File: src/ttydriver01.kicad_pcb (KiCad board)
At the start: 2 copper layers, 119.4 x 74.9 mm, 34 parts, among them P1 CONN_01X04, P2 CONN_01X02, P3 CONN_01X02, P4 CONN_01X10, Q1 IRLB8721PBF, T1 Coilcraft-DA2032, U1 NE555, U2 TPS2030P, U3 CP2102-breakout, U4 G3VM401E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

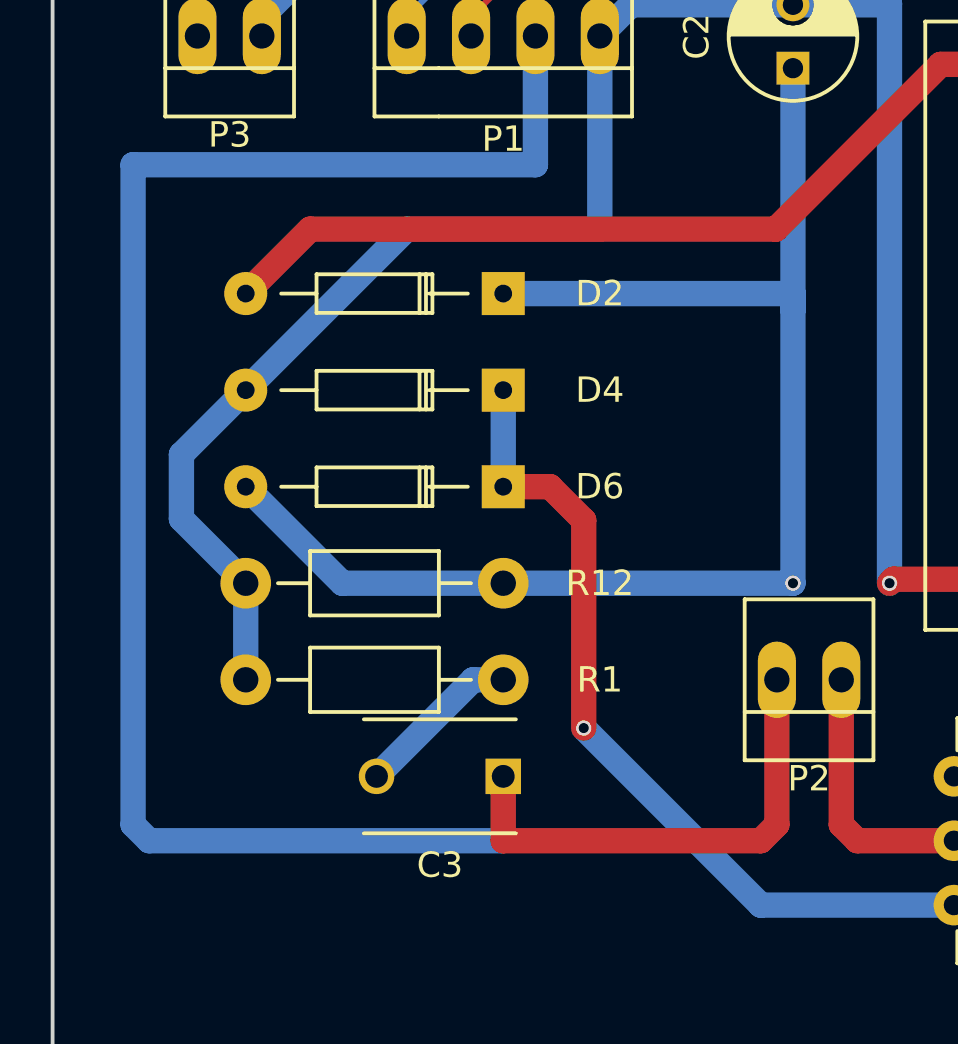
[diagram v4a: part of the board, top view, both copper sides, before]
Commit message: Change resistor R12 to unused R8
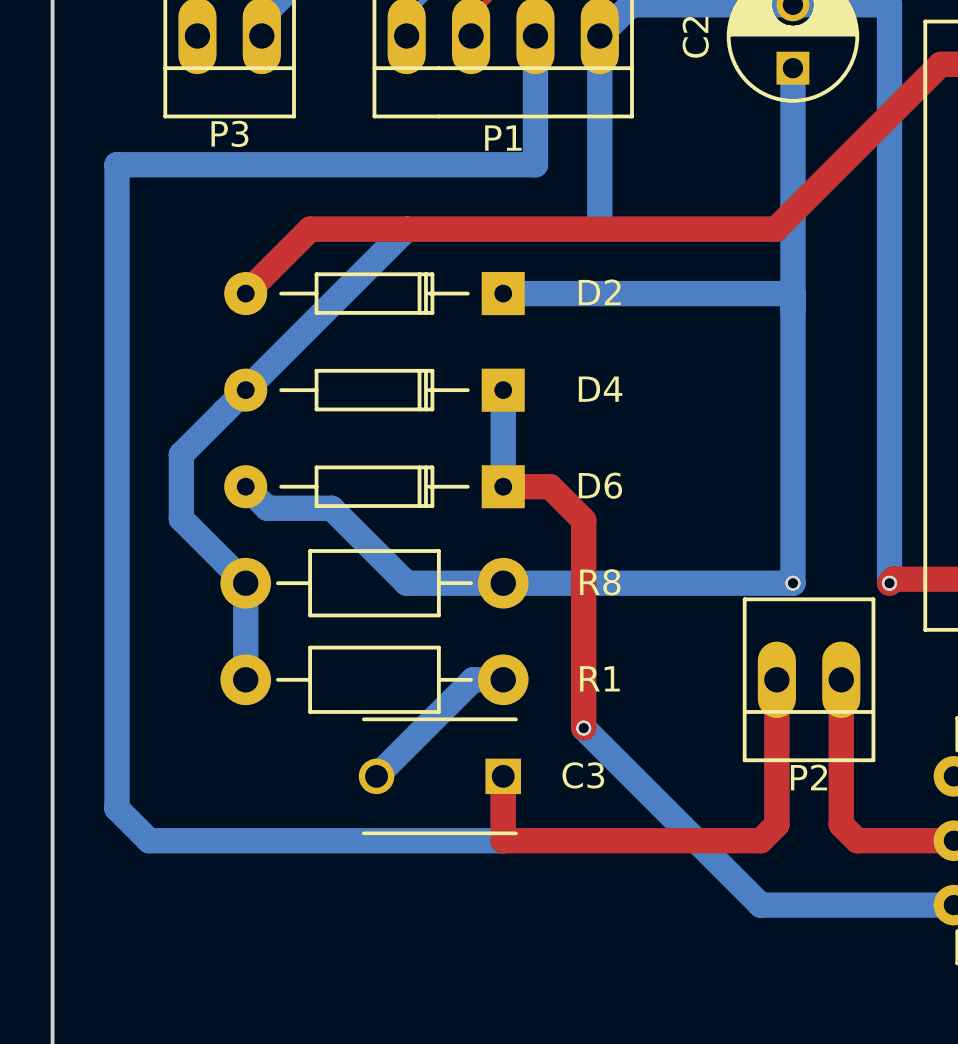
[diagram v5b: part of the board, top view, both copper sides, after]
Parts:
- removed R12: 1M, Resistors_ThroughHole:Resistor_Horizontal_RM10mm
- added R8: 1M, Resistors_ThroughHole:Resistor_Horizontal_RM10mm, F.Cu at (73.7, 130.8)
- R10, R11: value 670 -> 680
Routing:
- net /HVPOS: track 83.7 -> 84.6 mm
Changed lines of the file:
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@@
     (links 78)
     (no_connects 0)
-    (area 55.804999 77.394999 175.335001 152.475001)
+    (area 55.404999 77.394999 193.291156 167.760001)
     (thickness 1.6)
     (drawings 8)
-    (tracks 316)
+    (tracks 319)
     (zones 0)
     (modules 34)
@@
       (effects (font (size 1 1) (thickness 0.15)))
     )
-    (fp_text value 670 (at 5.08 0) (layer F.Fab)
+    (fp_text value 680 (at 5.08 0) (layer F.Fab)
       (effects (font (size 1 1) (thickness 0.15)))
     )
@@
       (effects (font (size 1 1) (thickness 0.15)))
     )
-    (fp_text value 670 (at 5.08 0) (layer F.Fab)
+    (fp_text value 680 (at 5.08 0) (layer F.Fab)
       (effects (font (size 1 1) (thickness 0.15)))
     )
@@
     (pad 2 thru_hole circle (at 10.16 0) (size 1.99898 1.99898) (drill 1.00076) (layers *.Cu *.SilkS *.Mask)
       (net 38 "Net-(P4-Pad9)"))
-    (model Resistors_ThroughHole.3dshapes/Resistor_Horizontal_RM10mm.wrl
-      (at (xyz 0.2 0 0))
-      (scale (xyz 0.4 0.4 0.4))
-      (rotate (xyz 0 0 0))
-    )
-  )
-  (module Resistors_ThroughHole:Resistor_Horizontal_RM10mm (layer F.Cu)
-    (at 73.66 130.81 180)
-    (descr "Resistor, Axial,  RM 10mm, 1/3W")
-    (tags "Resistor Axial RM 10mm 1/3W")
-    (fp_text reference R12 (at -3.81 0 180) (layer F.SilkS)
-      (effects (font (size 1 1) (thickness 0.15)))
-    )
-    (fp_text value 1M (at 5.08 0 180) (layer F.Fab)
-      (effects (font (size 1 1) (thickness 0.15)))
-    )
-    (fp_line (start -1.25 -1.5) (end 11.4 -1.5) (layer F.CrtYd) (width 0.05))
-    (fp_line (start -1.25 1.5) (end -1.25 -1.5) (layer F.CrtYd) (width 0.05))
-    (fp_line (start 11.4 -1.5) (end 11.4 1.5) (layer F.CrtYd) (width 0.05))
-    (fp_line (start -1.25 1.5) (end 11.4 1.5) (layer F.CrtYd) (width 0.05))
-    (fp_line (start 2.54 -1.27) (end 7.62 -1.27) (layer F.SilkS) (width 0.15))
-    (fp_line (start 7.62 -1.27) (end 7.62 1.27) (layer F.SilkS) (width 0.15))
-    (fp_line (start 7.62 1.27) (end 2.54 1.27) (layer F.SilkS) (width 0.15))
-    (fp_line (start 2.54 1.27) (end 2.54 -1.27) (layer F.SilkS) (width 0.15))
-    (fp_line (start 2.54 0) (end 1.27 0) (layer F.SilkS) (width 0.15))
-    (fp_line (start 7.62 0) (end 8.89 0) (layer F.SilkS) (width 0.15))
-    (pad 1 thru_hole circle (at 0 0 180) (size 1.99898 1.99898) (drill 1.00076) (layers *.Cu *.SilkS *.Mask)
-      (net 22 "Net-(C2-Pad1)"))
-    (pad 2 thru_hole circle (at 10.16 0 180) (size 1.99898 1.99898) (drill 1.00076) (layers *.Cu *.SilkS *.Mask)
-      (net 40 /HVNEG))
     (model Resistors_ThroughHole.3dshapes/Resistor_Horizontal_RM10mm.wrl
       (at (xyz 0.2 0 0))
@@
     (descr "Capacitor 6mm Disc, Pitch 5mm")
     (tags Capacitor)
-    (fp_text reference C3 (at 2.5 -3.5 180) (layer F.SilkS)
-      (effects (font (size 1 1) (thickness 0.15)))
-    )
-    (fp_text value 1000pf (at 2.5 3.5 180) (layer F.Fab)
+    (fp_text reference C3 (at -3.175 0 180) (layer F.SilkS)
+      (effects (font (size 1 1) (thickness 0.15)))
+    )
+    (fp_text value 1000pf (at 10.16 0 180) (layer F.Fab)
       (effects (font (size 1 1) (thickness 0.15)))
     )
@@
       (at (xyz 0.0984252 0 0))
       (scale (xyz 1 1 1))
+      (rotate (xyz 0 0 0))
+    )
+  )
+  (module Resistors_ThroughHole:Resistor_Horizontal_RM10mm (layer F.Cu)
+    (at 73.66 130.81 180)
+    (descr "Resistor, Axial,  RM 10mm, 1/3W")
+    (tags "Resistor Axial RM 10mm 1/3W")
+    (fp_text reference R8 (at -3.81 0 180) (layer F.SilkS)
+      (effects (font (size 1 1) (thickness 0.15)))
+    )
+    (fp_text value 1M (at 5.08 0 180) (layer F.Fab)
+      (effects (font (size 1 1) (thickness 0.15)))
+    )
+    (fp_line (start -1.25 -1.5) (end 11.4 -1.5) (layer F.CrtYd) (width 0.05))
+    (fp_line (start -1.25 1.5) (end -1.25 -1.5) (layer F.CrtYd) (width 0.05))
+    (fp_line (start 11.4 -1.5) (end 11.4 1.5) (layer F.CrtYd) (width 0.05))
+    (fp_line (start -1.25 1.5) (end 11.4 1.5) (layer F.CrtYd) (width 0.05))
+    (fp_line (start 2.54 -1.27) (end 7.62 -1.27) (layer F.SilkS) (width 0.15))
+    (fp_line (start 7.62 -1.27) (end 7.62 1.27) (layer F.SilkS) (width 0.15))
+    (fp_line (start 7.62 1.27) (end 2.54 1.27) (layer F.SilkS) (width 0.15))
+    (fp_line (start 2.54 1.27) (end 2.54 -1.27) (layer F.SilkS) (width 0.15))
+    (fp_line (start 2.54 0) (end 1.27 0) (layer F.SilkS) (width 0.15))
+    (fp_line (start 7.62 0) (end 8.89 0) (layer F.SilkS) (width 0.15))
+    (pad 1 thru_hole circle (at 0 0 180) (size 1.99898 1.99898) (drill 1.00076) (layers *.Cu *.SilkS *.Mask)
+      (net 22 "Net-(C2-Pad1)"))
+    (pad 2 thru_hole circle (at 10.16 0 180) (size 1.99898 1.99898) (drill 1.00076) (layers *.Cu *.SilkS *.Mask)
+      (net 40 /HVNEG))
+    (model Resistors_ThroughHole.3dshapes/Resistor_Horizontal_RM10mm.wrl
+      (at (xyz 0.2 0 0))
+      (scale (xyz 0.4 0.4 0.4))
       (rotate (xyz 0 0 0))
     )
@@
   (segment (start 102.81 110.34) (end 105.31 110.34) (width 1) (layer F.Cu) (net 21) (status 30))
   (segment (start 100.31 110.34) (end 102.81 110.34) (width 1) (layer F.Cu) (net 21) (status 30))
+  (segment (start 63.49948 127.00254) (end 64.349109 127.852169) (width 1) (layer B.Cu) (net 22))
   (segment (start 85.09 120.015) (end 85.09 110.49) (width 1) (layer B.Cu) (net 22) (status 20))
-  (via (at 85.09 130.81) (size 0.6) (drill 0.4) (layers F.Cu B.Cu) (net 22))
-  (segment (start 73.66 130.81) (end 67.31 130.81) (width 1) (layer B.Cu) (net 22) (status 10))
-  (segment (start 67.31 130.81) (end 63.50254 127.00254) (width 1) (layer B.Cu) (net 22) (status 20))
   (segment (start 63.50254 127.00254) (end 63.49948 127.00254) (width 1) (layer B.Cu) (net 22) (status 30))
   (segment (start 73.65948 119.38254) (end 85.09 119.38254) (width 1) (layer B.Cu) (net 22) (status 10))
   (segment (start 85.09 119.38254) (end 85.09 120.015) (width 1) (layer B.Cu) (net 22))
-  (segment (start 73.66 130.81) (end 85.09 130.81) (width 1) (layer B.Cu) (net 22) (status 10))
+  (segment (start 64.349109 127.852169) (end 66.892169 127.852169) (width 1) (layer B.Cu) (net 22))
   (segment (start 85.09 130.81) (end 85.09 120.015) (width 1) (layer B.Cu) (net 22))
+  (segment (start 85.09 130.81) (end 73.66 130.81) (width 1) (layer B.Cu) (net 22))
+  (segment (start 69.85 130.81) (end 73.66 130.81) (width 1) (layer B.Cu) (net 22))
+  (segment (start 66.892169 127.852169) (end 69.85 130.81) (width 1) (layer B.Cu) (net 22))
+  (via (at 85.09 130.81) (size 0.6) (drill 0.4) (layers F.Cu B.Cu) (net 22))
   (segment (start 73.66 134.62) (end 72.47 134.62) (width 1) (layer B.Cu) (net 23))
   (segment (start 72.47 134.62) (end 68.66 138.43) (width 1) (layer B.Cu) (net 23))
@@
   (segment (start 165.1 105.41) (end 166.099489 106.409489) (width 0.25) (layer B.Cu) (net 39) (status 10))
   (segment (start 166.099489 106.409489) (end 166.099489 126.635511) (width 0.25) (layer B.Cu) (net 39))
-  (segment (start 63.5 134.62) (end 63.5 130.81) (width 1) (layer B.Cu) (net 40) (status 30))
+  (segment (start 63.5 134.62) (end 63.5 130.81) (width 1) (layer B.Cu) (net 40))
+  (segment (start 63.5 130.81) (end 60.96 128.27) (width 1) (layer B.Cu) (net 40))
+  (segment (start 60.96 128.27) (end 60.96 125.73202) (width 1) (layer B.Cu) (net 40))
+  (segment (start 60.96 125.73202) (end 62.649851 124.042169) (width 1) (layer B.Cu) (net 40))
+  (segment (start 62.649851 124.042169) (end 63.49948 123.19254) (width 1) (layer B.Cu) (net 40))
   (segment (start 77.47 109.22) (end 77.47 116.84) (width 1) (layer B.Cu) (net 40) (status 10))
   (segment (start 77.47 116.84) (end 69.85202 116.84) (width 1) (layer B.Cu) (net 40))
   (segment (start 69.85202 116.84) (end 63.49948 123.19254) (width 1) (layer B.Cu) (net 40) (status 20))
-  (segment (start 63.49948 123.19254) (end 60.96202 125.73) (width 1) (layer B.Cu) (net 40) (status 10))
-  (segment (start 60.96202 125.73) (end 60.96202 128.27202) (width 1) (layer B.Cu) (net 40))
-  (segment (start 60.96202 128.27202) (end 63.5 130.81) (width 1) (layer B.Cu) (net 40) (status 20))
   (segment (start 85.09 107.99) (end 78.7 107.99) (width 1) (layer B.Cu) (net 40) (status 10))
   (segment (start 78.7 107.99) (end 77.47 109.22) (width 1) (layer B.Cu) (net 40) (status 20))
@@
   (segment (start 77.47 109.22) (end 77.47 108.92) (width 0.25) (layer B.Cu) (net 40) (status 30))
   (via (at 88.9 130.81) (size 0.6) (drill 0.4) (layers F.Cu B.Cu) (net 40))
+  (segment (start 74.93 109.22) (end 74.93 114.3) (width 1) (layer B.Cu) (net 41))
+  (segment (start 74.93 114.3) (end 58.42 114.3) (width 1) (layer B.Cu) (net 41))
+  (segment (start 58.42 114.3) (end 58.42 139.7) (width 1) (layer B.Cu) (net 41))
+  (segment (start 58.42 139.7) (end 59.69 140.97) (width 1) (layer B.Cu) (net 41))
+  (segment (start 59.69 140.97) (end 73.66 140.97) (width 1) (layer B.Cu) (net 41))
+  (segment (start 73.66 140.97) (end 73.66 138.43) (width 1) (layer B.Cu) (net 41))
   (segment (start 84.455 134.62) (end 84.455 140.335) (width 1) (layer F.Cu) (net 41) (status 10))
   (segment (start 84.455 140.335) (end 83.82 140.97) (width 1) (layer F.Cu) (net 41))
   (segment (start 83.82 140.97) (end 73.66 140.97) (width 1) (layer F.Cu) (net 41))
   (segment (start 73.66 140.97) (end 73.66 138.43) (width 1) (layer F.Cu) (net 41) (status 20))
-  (segment (start 73.66 140.97) (end 59.69 140.97) (width 1) (layer B.Cu) (net 41))
-  (segment (start 59.69 140.97) (end 59.055 140.335) (width 1) (layer B.Cu) (net 41))
-  (segment (start 59.055 114.3) (end 59.055 140.335) (width 1) (layer B.Cu) (net 41))
-  (segment (start 73.66 138.43) (end 73.66 140.97) (width 1) (layer B.Cu) (net 41) (status 10))
-  (segment (start 74.93 114.3) (end 59.055 114.3) (width 1) (layer B.Cu) (net 41))
-  (segment (start 74.93 109.22) (end 74.93 114.3) (width 1) (layer B.Cu) (net 41) (status 10))
   (segment (start 112.395 128.27) (end 124.46 128.27) (width 0.25) (layer F.Cu) (net 42))
   (segment (start 124.46 128.27) (end 130.81 134.62) (width 0.25) (layer F.Cu) (net 42))
